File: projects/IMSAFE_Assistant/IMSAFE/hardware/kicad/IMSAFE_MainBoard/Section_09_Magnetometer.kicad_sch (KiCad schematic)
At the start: 0 parts

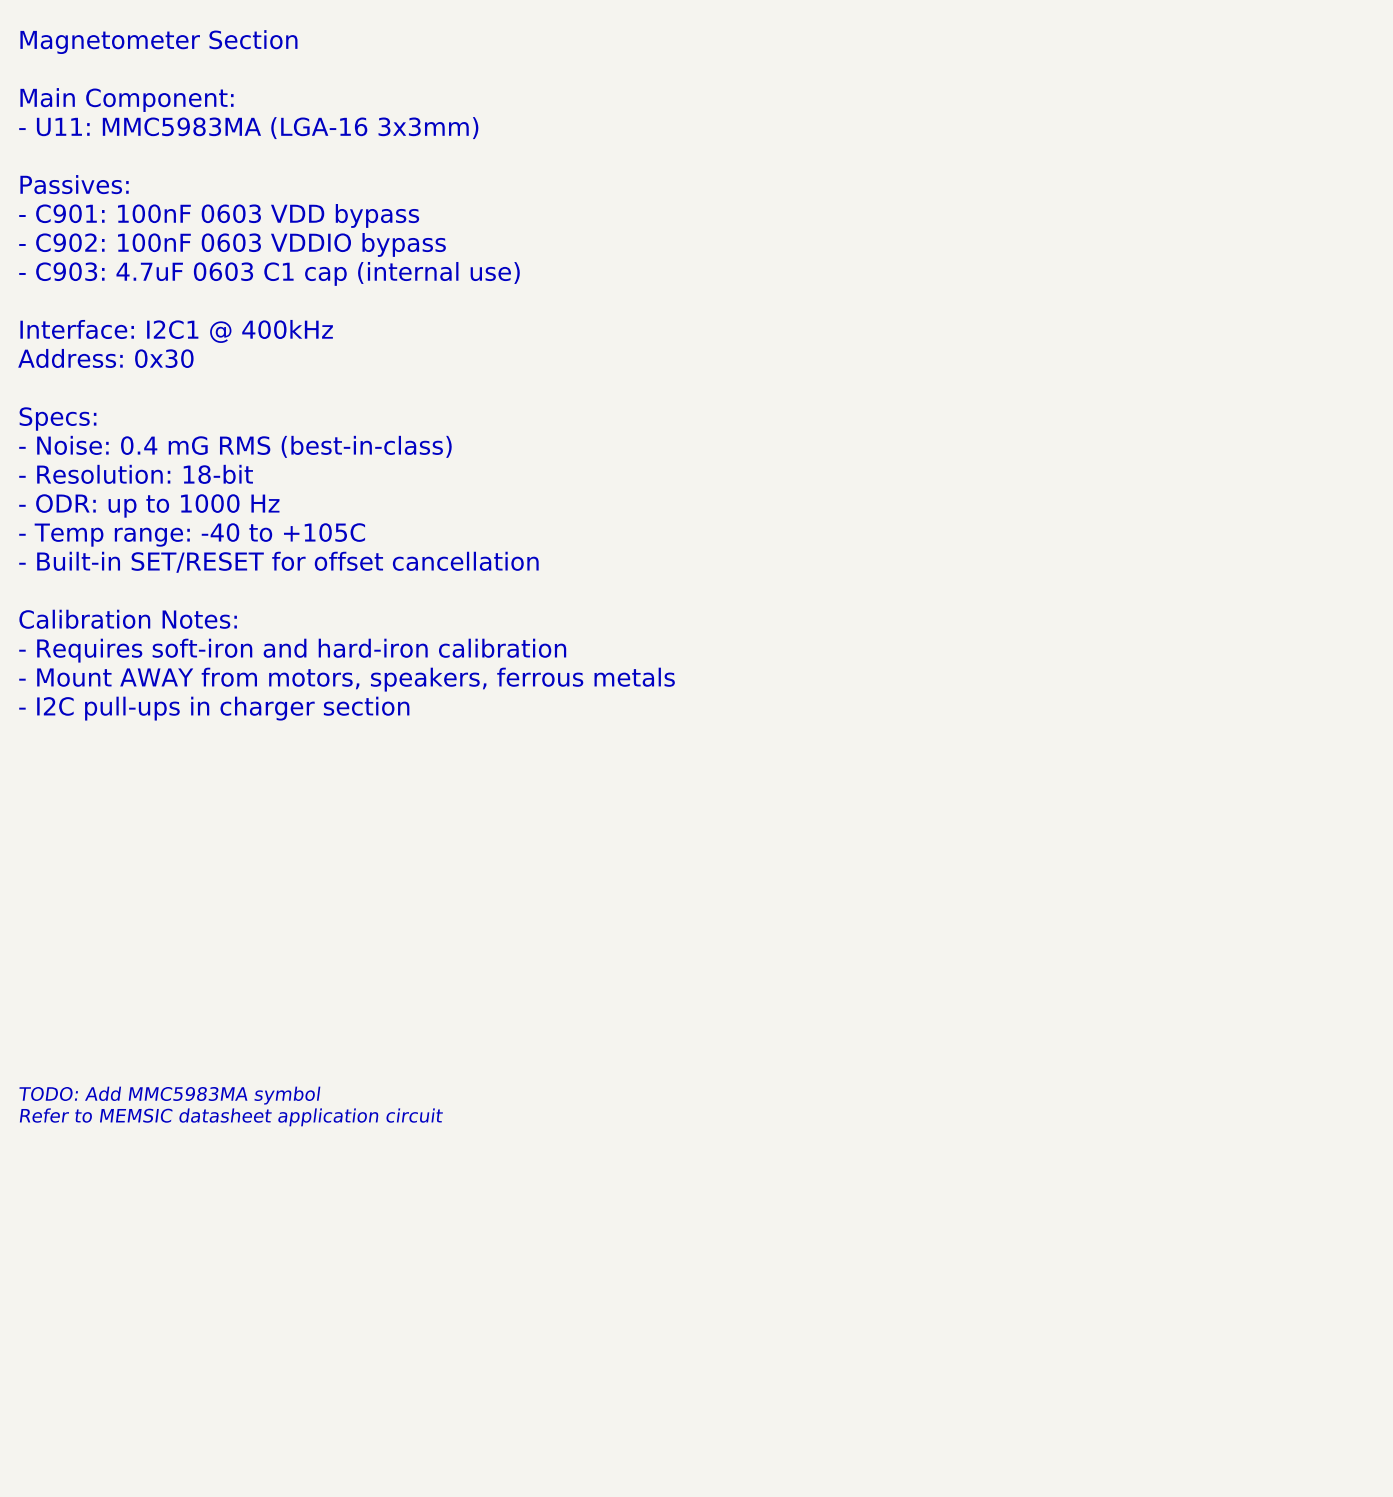
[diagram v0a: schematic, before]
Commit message: Add sensor and interface schematic implementations
- Section 01: MCU Core additional connections
- Section 04: BMS refinements
- Section 07: Barometric sensor (BMP390)
- Section 08: IMU (ICM-42688-P) full implementation
- Section 09: Magnetometer (MMC5983MA) full implementation
- Section 10: Gas sensor (MICS-4514) with heater control
- Section 11: Temp/Humidity (Si7021-A20) implementation
- Section 14: I/O Expander updates
- Section 16: Rotary encoder connections
- Section 19: Audio buzzer (MLT-8530) with MOSFET driver

Co-Authored-By: Claude Opus 4.5 <noreply@anthropic.com>
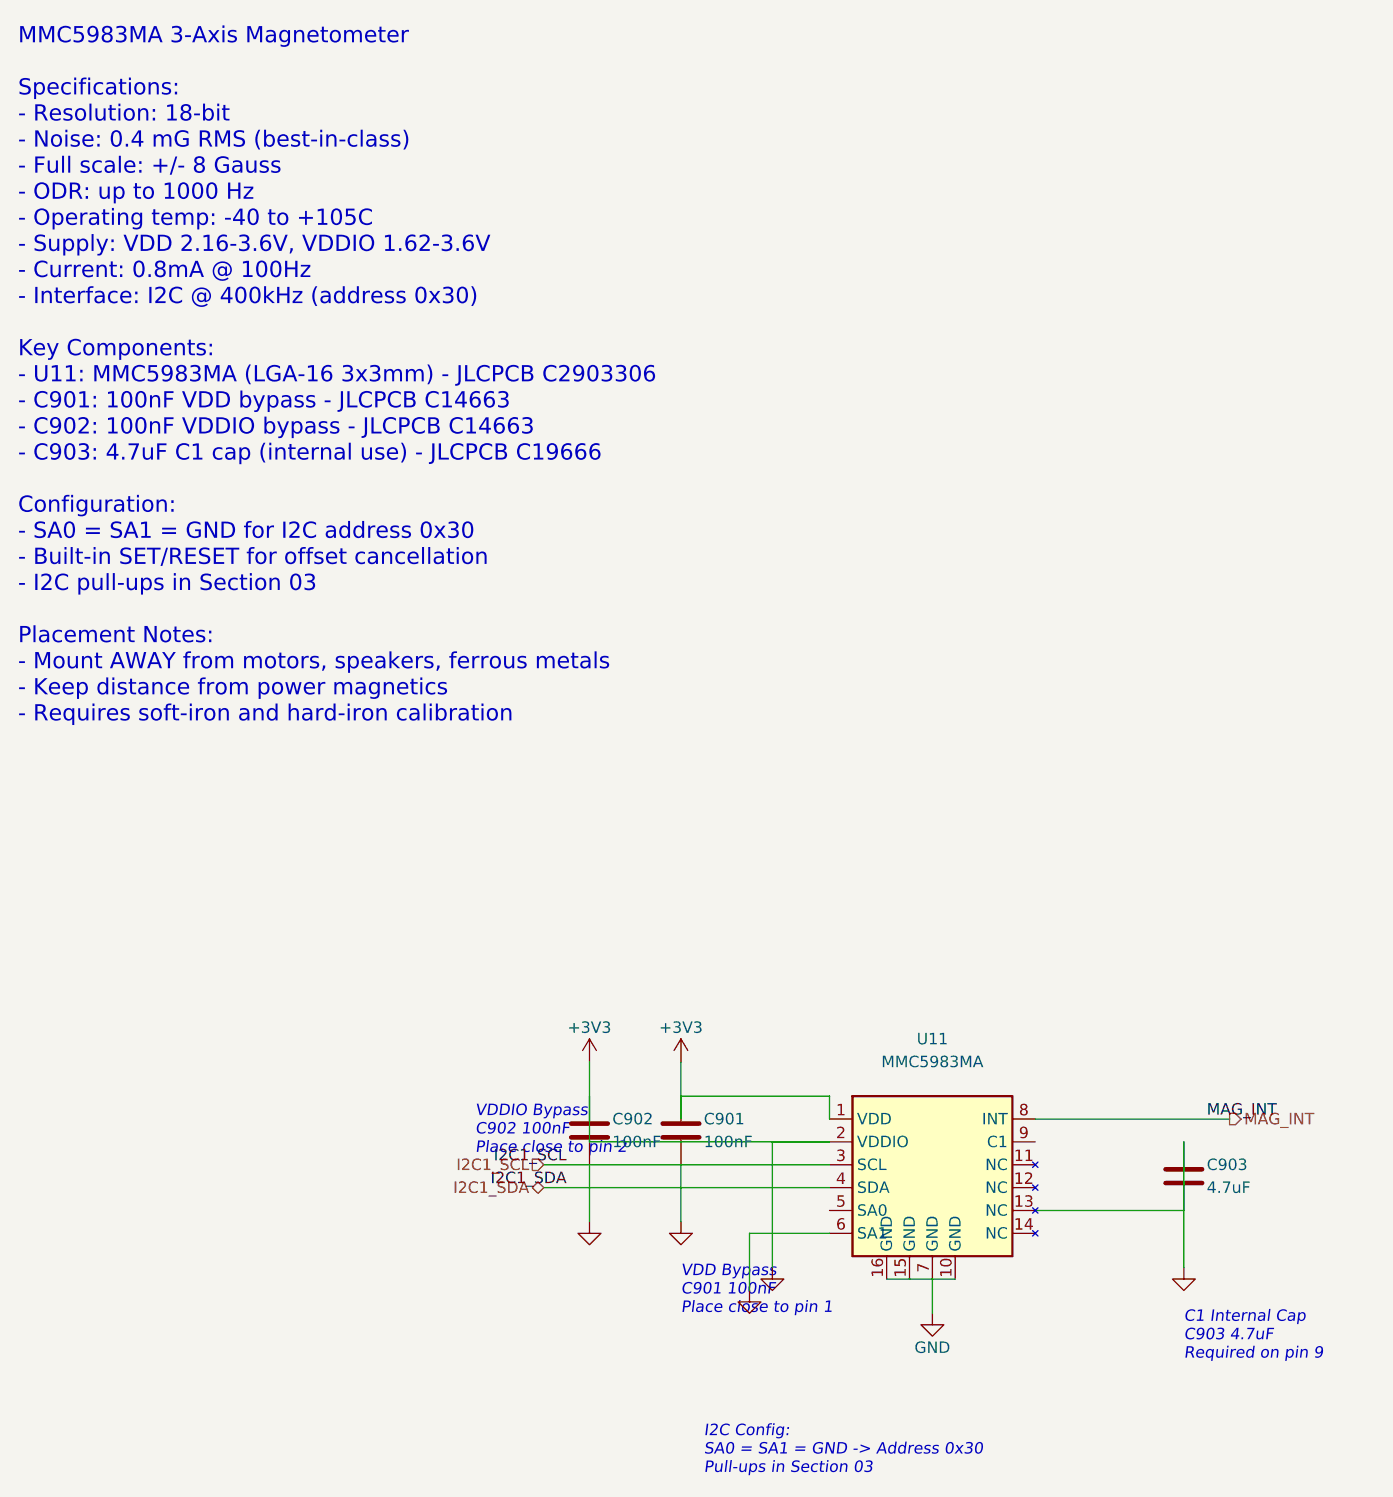
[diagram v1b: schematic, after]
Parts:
- added C901, C902: 100nF, Capacitor_SMD:C_0603_1608Metric, symbol Device:C
- added C903: 4.7uF, Capacitor_SMD:C_0603_1608Metric, symbol Device:C
- added U11: MMC5983MA, Package_LGA:LGA-16_3x3mm_P0.5mm, symbol Sensor:MMC5983MA
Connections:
- new net +3V3: C901.1, C901.2, C902.1, C902.2, C903.1, C903.2, U11.1 (VDD), U11.10 (GND), U11.13 (NC), U11.15 (GND), U11.16 (GND), U11.2 (VDDIO), U11.6 (SA1), U11.7 (GND)
- new net I2C1_SCL: U11.3 (SCL)
- new net I2C1_SDA: U11.4 (SDA)
- new net MAG_INT: U11.8 (INT)
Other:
- note added: "C1 Internal Cap C903 4.7uF Required on pin 9"
- note added: "I2C Config: SA0 = SA1 = GND -> Address 0x30 Pull-ups in Section 03"
- note added: "MMC5983MA 3-Axis Magnetometer Specifications: - Resolution: 18-bit - Noise: 0.4 mG RMS (best-in-class) - Full scale: +/- 8 Gauss - ODR: up to 1000 Hz - Operating temp: -40 to +105C - Supply: VDD 2.16-3.6V, VDDIO 1.62-3.6V - Current: 0.8mA @ 100Hz - Interface: I2C @ 400kHz (address 0x30) Key Components: - U11: MMC5983MA (LGA-16 3x3mm) - JLCPCB C2903306 - C901: 100nF VDD bypass - JLCPCB C14663 - C9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"
- note added: "VDD Bypass C901 100nF Place close to pin 1"
- note added: "VDDIO Bypass C902 100nF Place close to pin 2"
- note removed: "Magnetometer Section Main Component: - U11: MMC5983MA (LGA-16 3x3mm) Passives: - C901: 100nF 0603 VDD bypass - C902: 100nF 0603 VDDIO bypass - C903: 4.7uF 0603 C1 cap (internal use) Interface: I2C1 @ 400kHz Address: 0x30 Specs: - Noise: 0.4 mG RMS (best-in-class) - Resolution: 18-bit - ODR: up to 1000 Hz - Temp range: -40 to +105C - Built-in SET/RESET for offset cancellation Calibration Notes: - 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"
- note removed: "TODO: Add MMC5983MA symbol Refer to MEMSIC datasheet application circuit"

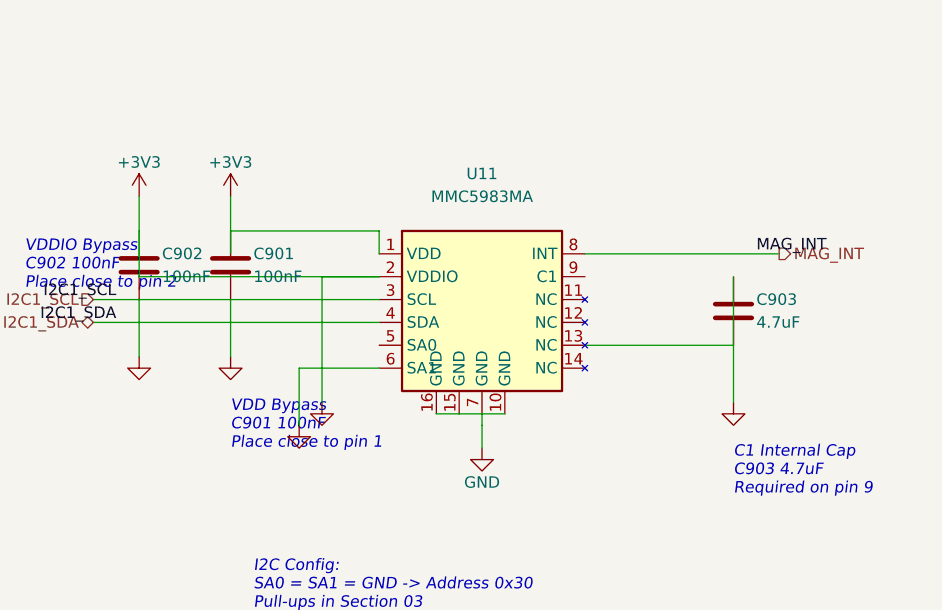
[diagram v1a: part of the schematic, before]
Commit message: Update KiCad schematics and add analysis files
- Update all MainBoard schematic sections with component placement
- Add ERC reports and analysis scripts for schematic validation
- Update Radar Interface and SwitchLED Board projects
- Sync KiCad project files with latest session changes

Co-Authored-By: Claude Opus 4.5 <noreply@anthropic.com>
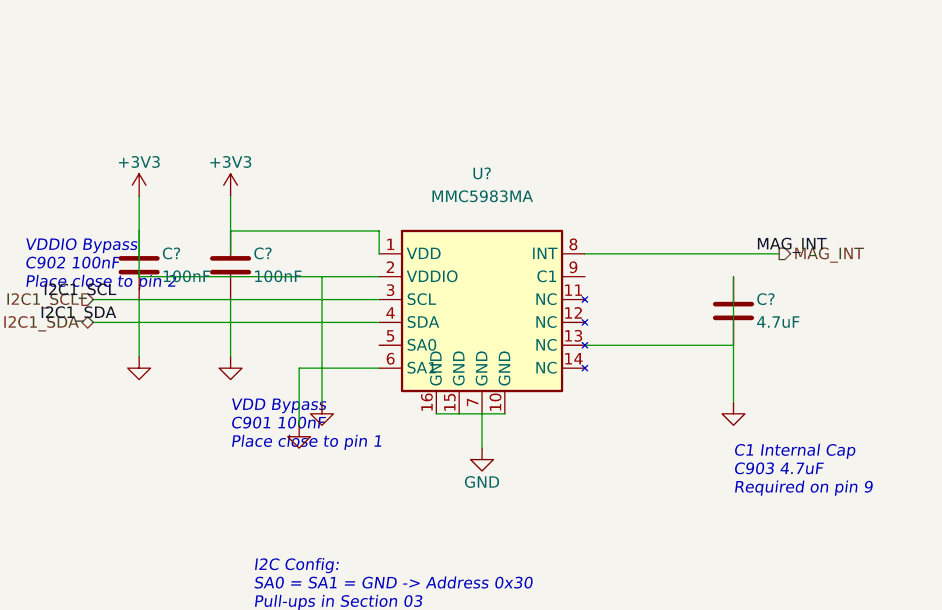
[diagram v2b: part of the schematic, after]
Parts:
- removed C901, C902: 100nF, Capacitor_SMD:C_0603_1608Metric, symbol Device:C
- removed C903: 4.7uF, Capacitor_SMD:C_0603_1608Metric, symbol Device:C
- removed U11: MMC5983MA, Package_LGA:LGA-16_3x3mm_P0.5mm, symbol Sensor:MMC5983MA
- added C? (x2): 100nF, Capacitor_SMD:C_0603_1608Metric, symbol Device:C
- added C?: 4.7uF, Capacitor_SMD:C_0603_1608Metric, symbol Device:C
- added U?: MMC5983MA, Package_LGA:LGA-16_3x3mm_P0.5mm, symbol Sensor:MMC5983MA
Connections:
- net +3V3: now also C?.1, C?.1, U?.1 (VDD), U?.2 (VDDIO)
- net I2C1_SCL: now also U?.3 (SCL)
- net I2C1_SDA: now also U?.4 (SDA)
- net MAG_INT: now also U?.8 (INT)
- new net GND: C?.1, C?.2, C?.2, C?.2, U?.10 (GND), U?.13 (NC), U?.15 (GND), U?.16 (GND), U?.6 (SA1), U?.7 (GND)
